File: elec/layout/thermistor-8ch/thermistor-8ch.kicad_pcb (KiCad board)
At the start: 4 copper layers, 29.7 x 28.3 mm, 78 parts, among them U5 10µH ±20%

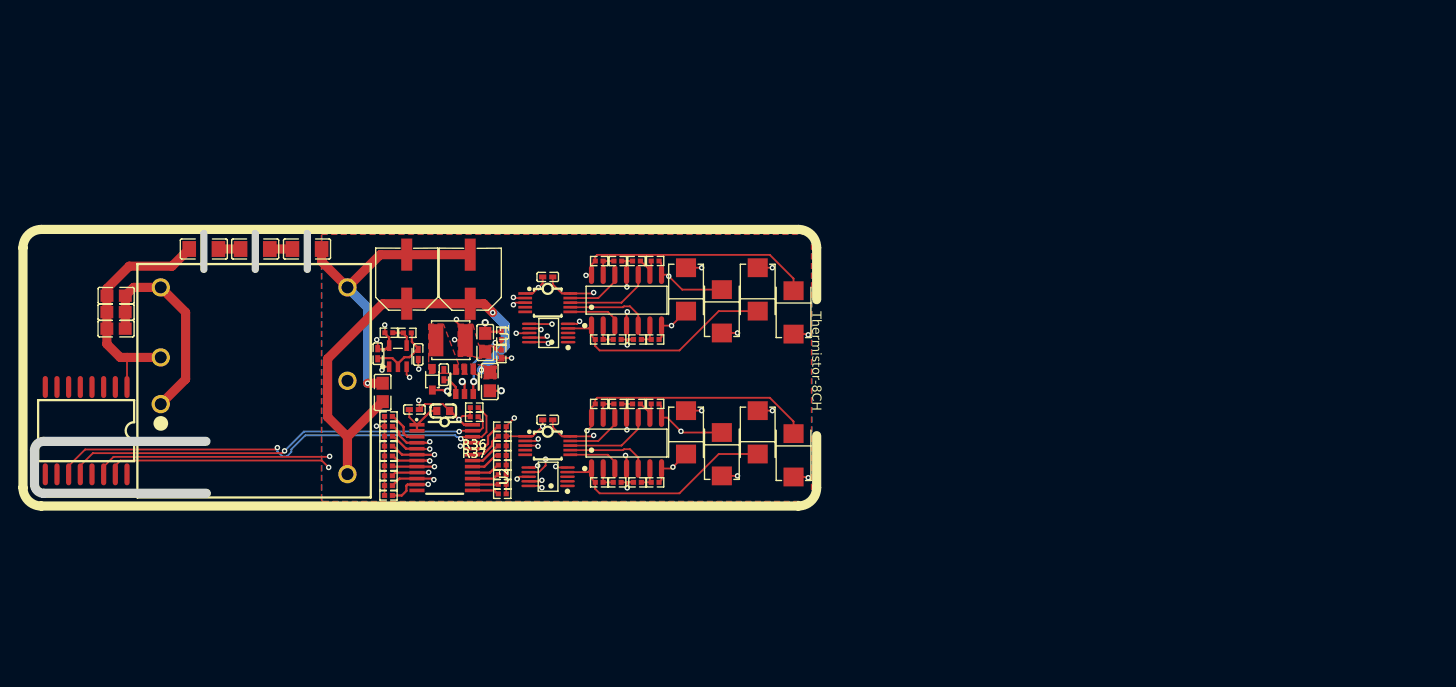
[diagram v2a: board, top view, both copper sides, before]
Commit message: add ATX core block
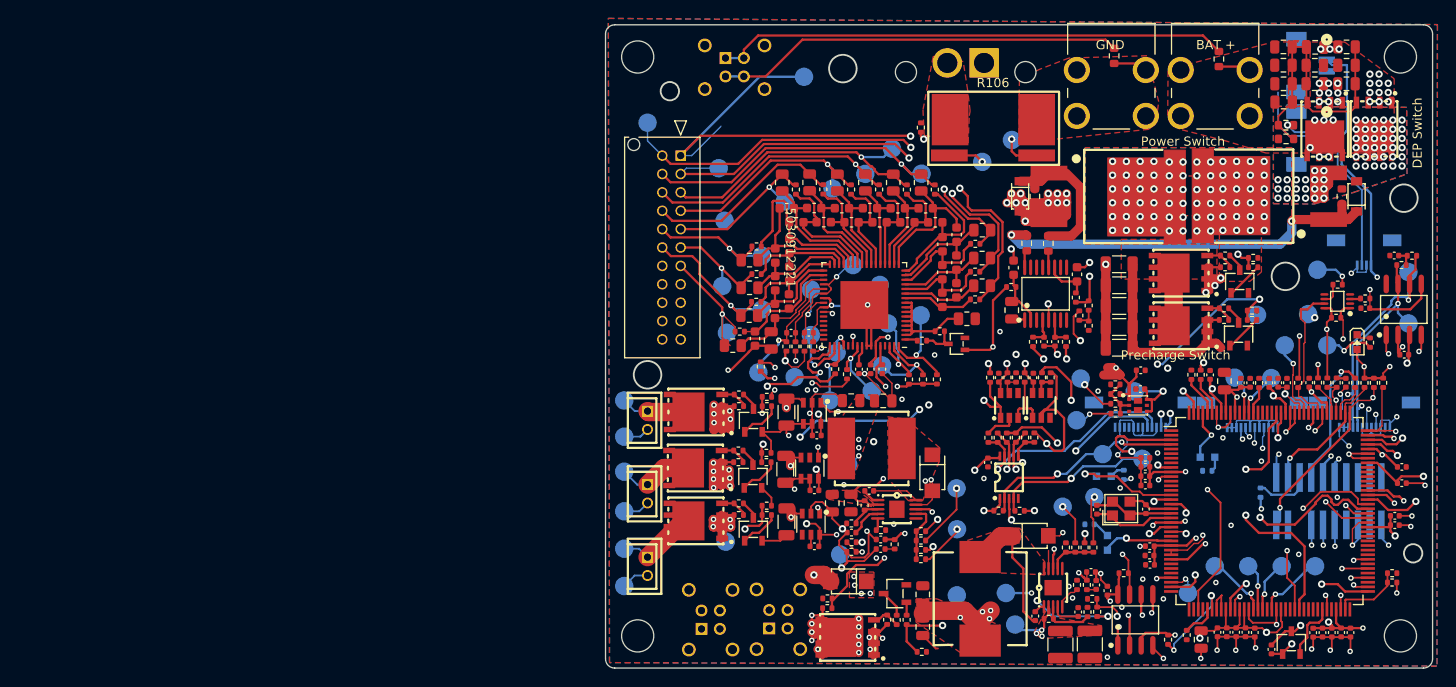
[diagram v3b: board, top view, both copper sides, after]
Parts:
- removed D5, D6, D7, D8: , atopile:SMB_L4.6-W3.6-LS5.3-RD-330cb3
- added C100: 16V 100nF X7R ±10% 0402 Multilayer Ceramic Capacitors MLCC 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, lib:C0402, F.Cu at (174.6, 105.3)
- added C101: 16V 100nF X7R ±10% 0402 Multilayer Ceramic Capacitors MLCC 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, lib:C0402, F.Cu at (175.0, 112.9)
- added C102: 16V 100nF X7R ±10% 0402 Multilayer Ceramic Capacitors MLCC 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, lib:C0402, F.Cu at (194.9, 121.3)
- added C103: 16V 100nF X7R ±10% 0402 Multilayer Ceramic Capacitors MLCC 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, lib:C0402, F.Cu at (202.7, 91.0)
- added C104: 16V 100nF X7R ±10% 0402 Multilayer Ceramic Capacitors MLCC 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, lib:C0402, F.Cu at (198.5, 86.0)
- added C105: 50V 4.7nF X7R ±10% 0402 Multilayer Ceramic Capacitors MLCC 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, lib:C0402, F.Cu at (201.7, 80.2)
- added C106: 16V 100nF X7R ±10% 0402 Multilayer Ceramic Capacitors MLCC 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, lib:C0402, F.Cu at (157.4, 102.8)
- added C107: 16V 100nF X7R ±10% 0402 Multilayer Ceramic Capacitors MLCC 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, lib:C0402, F.Cu at (170.4, 116.7)
- added C108: 16V 100nF X7R ±10% 0402 Multilayer Ceramic Capacitors MLCC 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, lib:C0402, F.Cu at (158.6, 93.5)
- added C109: 16V 100nF X7R ±10% 0402 Multilayer Ceramic Capacitors MLCC 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, lib:C0402, F.Cu at (162.4, 93.5)
- added C19: 25V 1uF X5R ±10% 0402 Multilayer Ceramic Capacitors MLCC - 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, lib:C0402, F.Cu at (174.0, 94.8)
- added C20: 25V 1uF X5R ±10% 0402 Multilayer Ceramic Capacitors MLCC - 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, lib:C0402, F.Cu at (174.1, 92.7)
- added C21: 25V 10uF X5R ±10% 0805 Multilayer Ceramic Capacitors MLCC -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, lib:C0805, F.Cu at (150.3, 117.1)
- added C22: 25V 10uF X5R ±10% 0805 Multilayer Ceramic Capacitors MLCC -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, lib:C0805, F.Cu at (150.3, 120.6)
- added C23: ?, lib:C1210, F.Cu at (168.5, 122.6)
- added C24: ?, lib:C1210, F.Cu at (165.3, 122.6)
- added C25: 50V 10nF X7R ±10% 0402 Multilayer Ceramic Capacitors MLCC -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, lib:C0402, F.Cu at (167.3, 119.0)
- added C26: 16V 100nF X7R ±10% 0402 Multilayer Ceramic Capacitors MLCC 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, lib:C0402, F.Cu at (162.6, 119.5)
- added C27: 16V 68nF X7R ±10% 0402 Multilayer Ceramic Capacitors MLCC -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, lib:C0402, F.Cu at (169.2, 116.1)
- added C28: 50V 6.8nF X7R ±10% 0402 Multilayer Ceramic Capacitors MLCC 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, lib:C0402, F.Cu at (168.7, 114.7)
- added C29: 25V 1uF X5R ±10% 0402 Multilayer Ceramic Capacitors MLCC - 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, lib:C0402, F.Cu at (145.9, 92.6)
- added C30: 25V 1uF X5R ±10% 0402 Multilayer Ceramic Capacitors MLCC - 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, lib:C0402, F.Cu at (143.4, 92.6)
- added C31: 25V 1uF X5R ±10% 0402 Multilayer Ceramic Capacitors MLCC - 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, lib:C0402, F.Cu at (144.7, 92.6)
- added C32: 50V 10nF X7R ±10% 0603 Multilayer Ceramic Capacitors MLCC -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, lib:C0603, F.Cu at (135.8, 85.2)
- added C33: 50V 27nF X7R ±10% 0603 Multilayer Ceramic Capacitors MLCC -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, lib:C0603, F.Cu at (134.3, 86.3)
- added C34: 50V 100nF X7R ±10% 0805 Multilayer Ceramic Capacitors MLCC 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, lib:C0805, F.Cu at (133.8, 89.5)
- added C35: 50V 10nF X7R ±10% 0603 Multilayer Ceramic Capacitors MLCC -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, lib:C0603, F.Cu at (132.1, 89.3)
- added C36: 50V 10nF X7R ±10% 0603 Multilayer Ceramic Capacitors MLCC -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, lib:C0603, F.Cu at (135.8, 82.2)
- added C37: 50V 27nF X7R ±10% 0603 Multilayer Ceramic Capacitors MLCC -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, lib:C0603, F.Cu at (134.3, 83.3)
- added C38: 50V 10nF X7R ±10% 0603 Multilayer Ceramic Capacitors MLCC -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, lib:C0603, F.Cu at (135.8, 79.2)
- added C39: 50V 27nF X7R ±10% 0603 Multilayer Ceramic Capacitors MLCC -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, lib:C0603, F.Cu at (134.3, 80.2)
- added C40: 50V 10nF X7R ±10% 0603 Multilayer Ceramic Capacitors MLCC -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, lib:C0603, F.Cu at (136.6, 76.6)
- added C41: 50V 27nF X7R ±10% 0603 Multilayer Ceramic Capacitors MLCC -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, lib:C0603, F.Cu at (135.5, 75.1)
- added C42: 50V 10nF X7R ±10% 0603 Multilayer Ceramic Capacitors MLCC -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, lib:C0603, F.Cu at (139.6, 76.6)
- added C43: 50V 27nF X7R ±10% 0603 Multilayer Ceramic Capacitors MLCC -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, lib:C0603, F.Cu at (138.5, 75.1)
- added C44: 50V 10nF X7R ±10% 0603 Multilayer Ceramic Capacitors MLCC -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, lib:C0603, F.Cu at (142.6, 76.6)
- added C45: 50V 27nF X7R ±10% 0603 Multilayer Ceramic Capacitors MLCC -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, lib:C0603, F.Cu at (141.6, 75.1)
- added C46: 50V 10nF X7R ±10% 0603 Multilayer Ceramic Capacitors MLCC -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, lib:C0603, F.Cu at (145.6, 76.6)
- added C47: 50V 27nF X7R ±10% 0603 Multilayer Ceramic Capacitors MLCC -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, lib:C0603, F.Cu at (144.6, 75.1)
- added C48: 50V 10nF X7R ±10% 0603 Multilayer Ceramic Capacitors MLCC -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, lib:C0603, F.Cu at (148.7, 76.6)
- added C49: 50V 27nF X7R ±10% 0603 Multilayer Ceramic Capacitors MLCC -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, lib:C0603, F.Cu at (147.6, 75.1)
- added C50: 50V 10nF X7R ±10% 0603 Multilayer Ceramic Capacitors MLCC -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, lib:C0603, F.Cu at (151.7, 76.6)
- added C51: 50V 27nF X7R ±10% 0603 Multilayer Ceramic Capacitors MLCC -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, lib:C0603, F.Cu at (150.7, 75.1)
- added C52: 50V 10nF X7R ±10% 0603 Multilayer Ceramic Capacitors MLCC -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, lib:C0603, F.Cu at (152.5, 79.0)
- added C53: 50V 27nF X7R ±10% 0603 Multilayer Ceramic Capacitors MLCC -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, lib:C0603, F.Cu at (154.0, 78.0)
- added C54: 50V 10nF X7R ±10% 0603 Multilayer Ceramic Capacitors MLCC -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, lib:C0603, F.Cu at (152.5, 82.1)
- added C55: 50V 27nF X7R ±10% 0603 Multilayer Ceramic Capacitors MLCC -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, lib:C0603, F.Cu at (154.0, 81.0)
- added C56: 50V 10nF X7R ±10% 0603 Multilayer Ceramic Capacitors MLCC -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, lib:C0603, F.Cu at (152.5, 85.1)
- added C57: 50V 27nF X7R ±10% 0603 Multilayer Ceramic Capacitors MLCC -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, lib:C0603, F.Cu at (154.0, 84.0)
- added C58: ?, lib:R0805, F.Cu at (155.1, 87.1)
- added C59: 50V 10nF X7R ±10% 0402 Multilayer Ceramic Capacitors MLCC -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, lib:C0402, F.Cu at (137.9, 88.6)
- added C60: 50V 10nF X7R ±10% 0402 Multilayer Ceramic Capacitors MLCC -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, lib:C0402, F.Cu at (136.0, 88.6)
- added C61: 50V 10nF X7R ±10% 0603 Multilayer Ceramic Capacitors MLCC -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, lib:C0603, F.Cu at (160.2, 81.6)
- added C62: 50V 10nF X7R ±10% 0603 Multilayer Ceramic Capacitors MLCC -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, lib:C0603, F.Cu at (167.1, 82.3)
- added C63: 16V 100nF X7R ±10% 0402 Multilayer Ceramic Capacitors MLCC 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, lib:C0402, F.Cu at (163.5, 89.6)
- added C64: 16V 100nF X7R ±10% 0402 Multilayer Ceramic Capacitors MLCC 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, lib:C0402, F.Cu at (164.7, 89.6)
- added C65: 50V 1uF X7R ±10% 0805 Multilayer Ceramic Capacitors MLCC - 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, lib:C0805, F.Cu at (160.0, 86.2)
- added C66: 25V 1uF X5R ±10% 0402 Multilayer Ceramic Capacitors MLCC - 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, lib:C0402, F.Cu at (138.6, 111.9)
- added C67: 25V 1uF X5R ±10% 0402 Multilayer Ceramic Capacitors MLCC - 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, lib:C0402, F.Cu at (138.6, 105.8)
- added C68: 25V 1uF X5R ±10% 0402 Multilayer Ceramic Capacitors MLCC - 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, lib:C0402, F.Cu at (138.8, 99.8)
- added C69: 16V 100nF X7R ±10% 0402 Multilayer Ceramic Capacitors MLCC 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, lib:C0402, F.Cu at (188.3, 123.1)
- added C70: 50V 20pF C0G ±5% 0402 Multilayer Ceramic Capacitors MLCC - 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, lib:C0402, F.Cu at (169.3, 107.9)
- added C71: 50V 20pF C0G ±5% 0402 Multilayer Ceramic Capacitors MLCC - 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, lib:C0402, F.Cu at (174.6, 107.8)
- added C72: 16V 100nF X7R ±10% 0402 Multilayer Ceramic Capacitors MLCC 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, lib:C0402, F.Cu at (174.6, 102.3)
- added C73: 50V 20pF C0G ±5% 0402 Multilayer Ceramic Capacitors MLCC - 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, lib:C0402, F.Cu at (196.4, 94.1)
- added C74: 25V 22uF X5R ±20% 0805 Multilayer Ceramic Capacitors MLCC -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, lib:C0805, F.Cu at (180.6, 122.0)
- added C75: 16V 100nF X7R ±10% 0402 Multilayer Ceramic Capacitors MLCC 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, lib:C0402, F.Cu at (192.4, 94.1)
- added C76: 16V 100nF X7R ±10% 0402 Multilayer Ceramic Capacitors MLCC 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, lib:C0402, F.Cu at (186.5, 121.3)
- added C77: 16V 100nF X7R ±10% 0402 Multilayer Ceramic Capacitors MLCC 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, lib:C0402, F.Cu at (188.0, 94.1)
- added C78: 16V 100nF X7R ±10% 0402 Multilayer Ceramic Capacitors MLCC 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, lib:C0402, F.Cu at (181.6, 93.2)
- added C79: 16V 100nF X7R ±10% 0402 Multilayer Ceramic Capacitors MLCC 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, lib:C0402, F.Cu at (201.7, 109.6)
- added C80: 16V 100nF X7R ±10% 0402 Multilayer Ceramic Capacitors MLCC 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, lib:C0402, F.Cu at (201.7, 108.6)
- added C81: 16V 100nF X7R ±10% 0402 Multilayer Ceramic Capacitors MLCC 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, lib:C0402, F.Cu at (184.4, 121.2)
- added C82: 16V 100nF X7R ±10% 0402 Multilayer Ceramic Capacitors MLCC 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, lib:C0402, F.Cu at (183.4, 121.2)
- added C83: 16V 100nF X7R ±10% 0402 Multilayer Ceramic Capacitors MLCC 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, lib:C0402, F.Cu at (182.4, 121.2)
- added C84: 16V 100nF X7R ±10% 0402 Multilayer Ceramic Capacitors MLCC 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, lib:C0402, F.Cu at (202.5, 105.0)
- added C85: 16V 100nF X7R ±10% 0402 Multilayer Ceramic Capacitors MLCC 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, lib:C0402, F.Cu at (185.5, 121.2)
- added C86: 25V 22uF X5R ±20% 0805 Multilayer Ceramic Capacitors MLCC -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, lib:C0805, F.Cu at (183.2, 93.9)
- added C87: 16V 100nF X7R ±10% 0402 Multilayer Ceramic Capacitors MLCC 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, lib:C0402, F.Cu at (174.6, 103.2)
- added C88: 16V 100nF X7R ±10% 0402 Multilayer Ceramic Capacitors MLCC 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, lib:C0402, F.Cu at (175.1, 113.9)
- added C89: 16V 100nF X7R ±10% 0402 Multilayer Ceramic Capacitors MLCC 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, lib:C0402, F.Cu at (193.8, 121.3)
- added C90: 16V 100nF X7R ±10% 0402 Multilayer Ceramic Capacitors MLCC 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, lib:C0402, F.Cu at (185.0, 94.1)
- added C91: 16V 100nF X7R ±10% 0402 Multilayer Ceramic Capacitors MLCC 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, lib:C0402, F.Cu at (192.8, 121.3)
- added C92: 16V 100nF X7R ±10% 0402 Multilayer Ceramic Capacitors MLCC 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, lib:C0402, F.Cu at (186.0, 94.1)
- added C93: 16V 100nF X7R ±10% 0402 Multilayer Ceramic Capacitors MLCC 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, lib:C0402, F.Cu at (202.5, 103.2)
- added C94: 16V 100nF X7R ±10% 0402 Multilayer Ceramic Capacitors MLCC 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, lib:C0402, F.Cu at (189.0, 94.1)
- added C95: 16V 100nF X7R ±10% 0402 Multilayer Ceramic Capacitors MLCC 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, lib:C0402, F.Cu at (195.9, 121.3)
- added C96: 16V 100nF X7R ±10% 0402 Multilayer Ceramic Capacitors MLCC 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, lib:C0402, F.Cu at (190.0, 94.1)
- added C97: 16V 100nF X7R ±10% 0402 Multilayer Ceramic Capacitors MLCC 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, lib:C0402, F.Cu at (196.9, 121.3)
- added C98: 16V 100nF X7R ±10% 0402 Multilayer Ceramic Capacitors MLCC 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, lib:C0402, F.Cu at (175.0, 111.9)
- added C99: 16V 100nF X7R ±10% 0402 Multilayer Ceramic Capacitors MLCC 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, lib:C0402, F.Cu at (174.6, 104.2)
- added DZ1: ?, lib:SOD-123_L2.7-W1.6-LS3.7-RD, F.Cu at (160.9, 73.8)
- added DZ2: ?, lib:SOD-123_L2.7-W1.6-LS3.7-RD, F.Cu at (197.6, 73.8)
- added J1: ?, lib:SAMTEC_FTR-110-03-G-D-06, B.Cu at (194.5, 107.0)
- added L1: ?, lib:IND-SMD_L8.0-W8.0_SMNR8040, F.Cu at (144.8, 101.2)
- added L2: ?, lib:IND-SMD_L10.1-W10.1_SMDRS1045, F.Cu at (156.6, 117.6)
- added LED1: ?, lib:LED0603-RD, B.Cu at (170.4, 111.5)
- added LED2: ?, lib:LED0603-RD, B.Cu at (170.1, 104.3)
- added Q1: ?, lib:POWERPAK-SO-8_L6.1-W5.1-P1.27-BL-EP, F.Cu at (199.5, 66.5)
- added Q10: ?, lib:SOT-23-3_L2.9-W1.6-P1.90-LS2.8-BR, F.Cu at (131.9, 110.0)
- added Q11: ?, lib:POWERPAK-SO-8_L6.1-W5.1-P1.27-BL-EP, F.Cu at (125.6, 103.4)
- added Q12: ?, lib:SOT-23-3_L2.9-W1.6-P1.90-LS2.8-BR, F.Cu at (131.9, 104.3)
- added Q13: ?, lib:POWERPAK-SO-8_L6.1-W5.1-P1.27-BL-EP, F.Cu at (125.7, 97.3)
- added Q14: ?, lib:SOT-23-3_L2.9-W1.6-P1.90-LS2.8-BR, F.Cu at (131.9, 98.2)
- added Q15: ?, lib:POWERPAK-SO-8_L6.1-W5.1-P1.27-BL-EP, F.Cu at (142.2, 121.8)
- added Q16: ?, lib:SOT-23-3_L2.9-W1.6-P1.90-LS2.8-BR, F.Cu at (147.3, 117.0)
- added Q2: ?, lib:POWERPAK-SO-8_L6.1-W5.1-P1.27-BL-EP, F.Cu at (194.1, 66.5)
- added Q3: ?, lib:TO-263-3_L10.1-W9.0-P5.08-LS15.2-BL-1, F.Cu at (189.2, 73.8)
- added Q4: ?, lib:TO-263-3_L10.1-W9.0-P5.08-LS15.2-BL-1, F.Cu at (169.4, 73.8)
- added Q5: ?, lib:POWERPAK-SO-8_L6.1-W5.1-P1.27-BL-EP, F.Cu at (178.5, 87.9)
- added Q6: ?, lib:SOT-23-3_L2.9-W1.6-P1.90-LS2.8-BR, F.Cu at (184.7, 88.8)
- added Q7: ?, lib:POWERPAK-SO-8_L6.1-W5.1-P1.27-BL-EP, F.Cu at (178.4, 82.2)
- added Q8: ?, lib:SOT-23-3_L2.9-W1.6-P1.90-LS2.8-BR, F.Cu at (184.8, 83.1)
- added Q9: ?, lib:POWERPAK-SO-8_L6.1-W5.1-P1.27-BL-EP, F.Cu at (125.7, 109.1)
- added R100: ?, lib:R1206, F.Cu at (135.4, 103.5)
- added R101: 62.5mW Thick Film Resistors 50V ±100ppm/℃ ±1% 39kΩ 0402 Chi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, lib:R0402, F.Cu at (130.3, 96.6)
- added R102: 62.5mW Thick Film Resistors 50V ±100ppm/℃ ±1% 120kΩ 0402 Ch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, lib:R0402, F.Cu at (130.3, 95.4)
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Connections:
- C1 pad 1: CB -> battery-vcc
- C1 pad 2: SW -> inhibit_switch-gate
- C10 pad 1: hv-2 -> battery-vcc
- C10 pad 2: gnd -> inhibit_switch-gate
- C11 pad 1: hv-2 -> 1v2_vcc
- C12 pad 1: hv-2 -> 1v2_vcc
- C13 pad 1: hv-4 -> 5v_vcc
- C13 pad 2: gnd-1 -> gnd
- C14 pad 1: hv-4 -> 5v_vcc
- C14 pad 2: gnd-1 -> gnd
- C15 pad 1: hv-4 -> power_supply_1v2.ic-ss_tr
- C15 pad 2: gnd-1 -> gnd
- C16 pad 1: gnd -> power_supply_1v2.ic-boot
- C16 pad 2: regulator_24v_isolated-net-1 -> power_supply_1v2.ic-ph
- C17 pad 1: regulator_24v_isolated-net-1 -> power_supply_1v2.r_comp-vcc
- C17 pad 2: regulator_24v_isolated-net -> gnd
- C18 pad 1: regulator_24v_isolated-net -> power_supply_1v2.ic-comp
- C18 pad 2: gnd-1 -> gnd
- C2 pad 1: hv-4 -> battery-vcc
- C2 pad 2: gnd-1 -> inhibit_switch-gate
- C3 pad 1: hv -> battery-vcc
- C3 pad 2: gnd-1 -> inhibit_switch-gate
- C4 pad 1: hv-1 -> battery-vcc
- C4 pad 2: gnd-1 -> inhibit_switch-gate
- C5 pad 1: hv-1 -> battery-vcc
- C5 pad 2: gnd-1 -> inhibit_switch-gate
- C6 pad 1: hv-1 -> battery-vcc
- C6 pad 2: gnd-1 -> inhibit_switch-gate
- C7 pad 1: hv-1 -> battery-vcc
- C7 pad 2: gnd-1 -> inhibit_switch-gate
- C8 pad 1: hv -> battery-vcc
- C8 pad 2: gnd-1 -> inhibit_switch-gate
- C9 pad 1: hv-1 -> battery-vcc
- C9 pad 2: gnd-1 -> inhibit_switch-gate
- D1 pad 1: line-8 -> power_supply_1v2.ic-ph
- D1 pad 2: gnd-1 -> gnd
- D2 pad 1: line-12 -> power_supply_5v.ic-ph
- D2 pad 2: gnd-1 -> gnd
- D3 pad 1: line-17 -> batt_inhibit_vcc
- D3 pad 2: gnd-1 -> (no net)
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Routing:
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- added copper zone on F.Cu, net 1v2_vcc
- added copper zone on In1.Cu, net 1v2_vcc
- added copper zone on In3.Cu, net 1v2_vcc
- added copper zone on In2.Cu, net 3v3_vcc
- added copper zone on In4.Cu, net 3v3_vcc
- added copper zone on F.Cu, net 5v_vcc
- added copper zone on B.Cu, net batt_inhibit_vcc
- added copper zone on F.Cu, net batt_inhibit_vcc
- added copper zone on In1.Cu, net batt_inhibit_vcc
- added copper zone on In1.Cu, net batt_sat_vcc
- added copper zone on In2.Cu, net batt_sat_vcc
- added copper zone on In1.Cu, net batt_share_vcc
- added copper zone on In2.Cu, net batt_share_vcc
- added copper zone on F.Cu, net batt_system_vcc
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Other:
- board size 29.7 x 28.3 mm -> 90 x 70 mm
- copper layers 4 -> 6
- board text added: "1V2"
- board text added: "5V"
- board text added: "BAT +"
- board text added: "Batt Sense"
- board text added: "C0"
- board text added: "C1"
- board text added: "C10"
- board text added: "C11"
- board text added: "C12"
- board text added: "C2"
- board text added: "C4"
- board text added: "C5"
- board text added: "C6"
- board text added: "C7"
- board text added: "C8"
- board text added: "C9"
- board text added: "CAN"
- board text added: "CANH"
- board text added: "CANL"
- board text added: "CS"
- board text added: "DEBUG"
- board text added: "DEP"
- board text added: "DEP Switch"
- board text added: "ECLK"
- board text added: "GND"
- board text added: "Housekeeper"
- board text added: "I1N"
- board text added: "I1P"
- board text added: "I2N"
- board text added: "I2P"
- board text added: "Inhibit"
- board text added: "MISO"
- board text added: "MOSI"
- board text added: "MPSpace"
- board text added: "PCDU"
- board text added: "POR"
- board text added: "Power Switch"
- board text added: "Precharge Switch"
- board text added: "REV04.1"
- board text added: "RST"
- board text added: "RX"
- board text added: "SCK"
- board text added: "SCL"
- board text added: "SDA"
- board text added: "SEP"
- board text added: "SERIAL"
- board text added: "SHNTN"
- board text added: "SHNTP"
- board text added: "SPI1"
- board text added: "SPI3"
- board text added: "STATUS"
- board text added: "T0"
- board text added: "T1"
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
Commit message: remove omron relay, fix thermistor layout
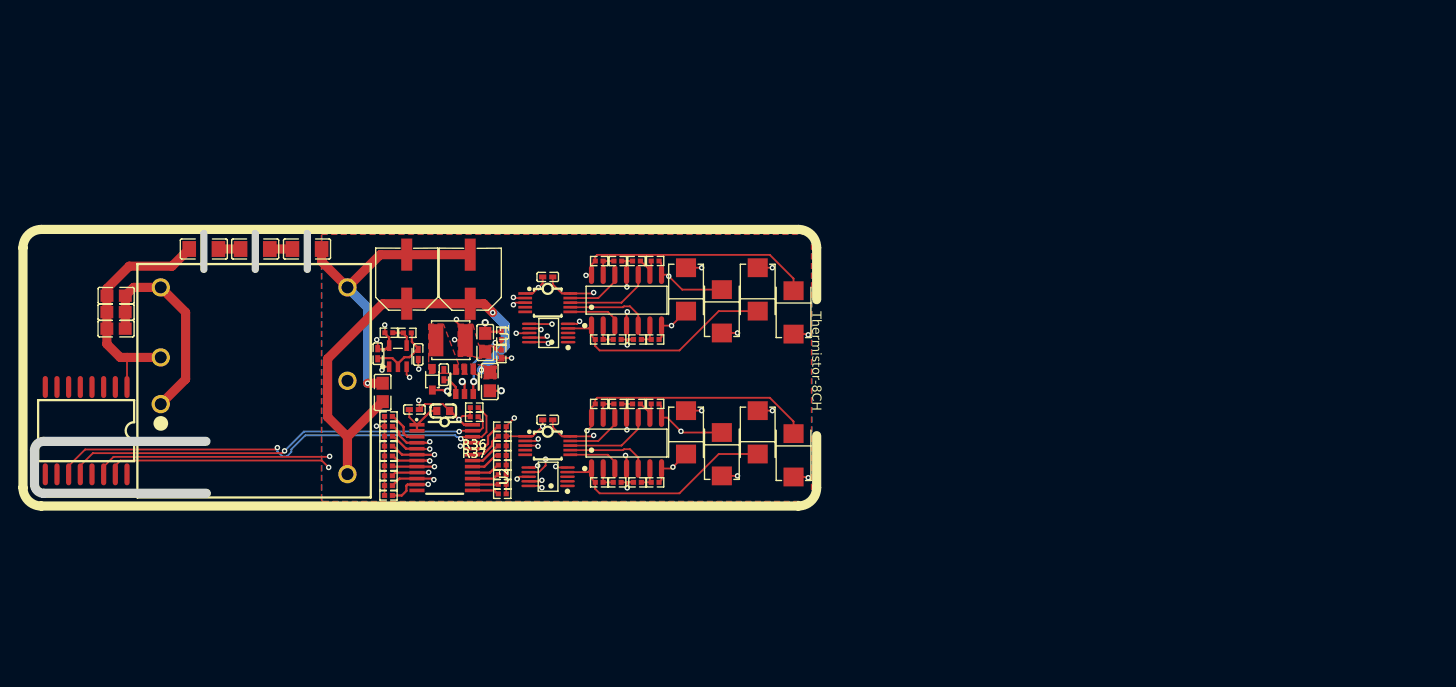
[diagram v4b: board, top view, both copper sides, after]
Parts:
- removed C100, C101, C102, C103, C104, C106, C107, C108, C109, C26, C63, C64, C69, C72, C75, C76, C77, C78, C79, C80, C81, C82, C83, C84, C85, C87, C88, C89, C90, C91, C92, C93, C94, C95, C96, C97, C98, C99: 16V 100nF X7R ±10% 0402 Multilayer Ceramic Capacitors MLCC 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, lib:C0402
- removed C105: 50V 4.7nF X7R ±10% 0402 Multilayer Ceramic Capacitors MLCC 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, lib:C0402
- removed C19, C20, C29, C30, C31, C66, C67, C68: 25V 1uF X5R ±10% 0402 Multilayer Ceramic Capacitors MLCC - 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, lib:C0402
- removed C21, C22: 25V 10uF X5R ±10% 0805 Multilayer Ceramic Capacitors MLCC -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, lib:C0805
- removed C23, C24: ?, lib:C1210
- removed C25, C59, C60: 50V 10nF X7R ±10% 0402 Multilayer Ceramic Capacitors MLCC -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, lib:C0402
- removed C27: 16V 68nF X7R ±10% 0402 Multilayer Ceramic Capacitors MLCC -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, lib:C0402
- removed C28: 50V 6.8nF X7R ±10% 0402 Multilayer Ceramic Capacitors MLCC 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, lib:C0402
- removed C32, C35, C36, C38, C40, C42, C44, C46, C48, C50, C52, C54, C56, C61, C62: 50V 10nF X7R ±10% 0603 Multilayer Ceramic Capacitors MLCC -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, lib:C0603
- removed C33, C37, C39, C41, C43, C45, C47, C49, C51, C53, C55, C57: 50V 27nF X7R ±10% 0603 Multilayer Ceramic Capacitors MLCC -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, lib:C0603
- removed C34: 50V 100nF X7R ±10% 0805 Multilayer Ceramic Capacitors MLCC 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, lib:C0805
- removed C58: ?, lib:R0805
- removed C65: 50V 1uF X7R ±10% 0805 Multilayer Ceramic Capacitors MLCC - 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, lib:C0805
- removed C70, C71, C73: 50V 20pF C0G ±5% 0402 Multilayer Ceramic Capacitors MLCC - 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, lib:C0402
- removed C74, C86: 25V 22uF X5R ±20% 0805 Multilayer Ceramic Capacitors MLCC -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, lib:C0805
- removed DZ1, DZ2: ?, lib:SOD-123_L2.7-W1.6-LS3.7-RD
- removed J1: ?, lib:SAMTEC_FTR-110-03-G-D-06
- removed L1: ?, lib:IND-SMD_L8.0-W8.0_SMNR8040
- removed L2: ?, lib:IND-SMD_L10.1-W10.1_SMDRS1045
- removed LED1, LED2, U83, U84: ?, lib:LED0603-RD
- removed Q1, Q11, Q13, Q15, Q2, Q5, Q7, Q9: ?, lib:POWERPAK-SO-8_L6.1-W5.1-P1.27-BL-EP
- removed Q10, Q12, Q14, Q16, Q6, Q8, U67: ?, lib:SOT-23-3_L2.9-W1.6-P1.90-LS2.8-BR
- removed Q3, Q4: ?, lib:TO-263-3_L10.1-W9.0-P5.08-LS15.2-BL-1
- removed R100, R105, R86, R87, R88, R89, R90, R95: ?, lib:R1206
- removed R101, R144, R78, R82, R91, R96: 62.5mW Thick Film Resistors 50V ±100ppm/℃ ±1% 39kΩ 0402 Chi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, lib:R0402
- removed R102, R145, R79, R83, R92, R97: 62.5mW Thick Film Resistors 50V ±100ppm/℃ ±1% 120kΩ 0402 Ch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, lib:R0402
- removed R103, R111, R112, R113, R115, R116, R117, R121, R122, R129, R130, R131, R134, R136, R146, R150, R151, R152, R153, R80, R84, R93, R98: 62.5mW Thick Film Resistors 50V ±100ppm/℃ ±1% 10kΩ 0402 Chi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, lib:R0402
- removed R104, R147, R81, R85, R94, R99: 62.5mW Thick Film Resistors 50V ±100ppm/℃ ±1% 1kΩ 0402 Chip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, lib:R0402
- removed R106: ?, lib:RES-SMD_4P-L10.8-W6.7
- removed R107, R108: 62.5mW Thick Film Resistors 50V ±1% ±100ppm/℃ 22Ω 0402 Chip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, lib:R0402
- removed R109, R118, R59, R70, R71: 62.5mW Thick Film Resistors 50V ±1% ±200ppm/℃ 100Ω 0402 Chi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, lib:R0402
- removed R110, R114, R72, R73: 62.5mW Thick Film Resistors 50V ±100ppm/℃ ±1% 4.7kΩ 0402 Ch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, lib:R0402
- removed R119, R120, R127, R128: 62.5mW Thick Film Resistors 50V ±100ppm/℃ ±1% 62Ω 0402 Chip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, lib:R0402
- removed R123, R124, R125, R126: 62.5mW Thick Film Resistors 50V ±100ppm/℃ ±1% 300Ω 0402 Chi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, lib:R0402
- removed R132: 62.5mW Thick Film Resistors 50V ±100ppm/℃ ±1% 28kΩ 0402 Chi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, lib:R0402
- removed R133, R64, R65, R66, R67, R68: 62.5mW Thick Film Resistors 50V ±100ppm/℃ ±1% 100kΩ 0402 Ch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, lib:R0402
- removed R135: 62.5mW Thick Film Resistors 50V ±100ppm/℃ ±1% 24.9kΩ 0402 C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, lib:R0402
- removed R137: 62.5mW Thick Film Resistors 50V ±800ppm/℃ ±1% 0Ω 0402 Chip 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, lib:R0402
- removed R138: 62.5mW Thick Film Resistors 50V ±100ppm/℃ ±1% 9.1kΩ 0402 Ch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, lib:R0402
- removed R139: 62.5mW Thick Film Resistors 50V ±100ppm/℃ ±1% 12.4kΩ 0402 C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, lib:R0402
- removed R140: 62.5mW Thick Film Resistors 50V ±100ppm/℃ ±1% 3.6kΩ 0402 Ch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, lib:R0402
- removed R141: 62.5mW Thick Film Resistors 50V ±100ppm/℃ ±1% 3.83kΩ 0402 C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, lib:R0402
- removed R142: 62.5mW Thick Film Resistors 50V ±100ppm/℃ ±1% 1.07MΩ 0402 C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, lib:R0402
- removed R143: 62.5mW Thick Film Resistors 50V ±100ppm/℃ ±1% 80.6kΩ 0402 C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, lib:R0402
- removed R148: 62.5mW Thick Film Resistors 50V ±100ppm/℃ ±1% 91kΩ 0402 Chi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, lib:R0402
- removed R149: 62.5mW Thick Film Resistors 50V ±100ppm/℃ ±1% 3.9kΩ 0402 Ch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, lib:R0402
- removed R40, R42, R44, R46, R48, R50, R52, R54, R56, R58: 125mW Thin Film Resistor 150V ±1% ±25ppm/℃ 80.6Ω 0805 Chip 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, lib:R0805
- removed R41, R43, R45, R47, R49, R51, R53, R55, R57, R60, R61, R62, R63: 62.5mW Thick Film Resistors 50V ±100ppm/℃ ±1% 200Ω 0402 Chi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, lib:R0402
- removed R69: ?, lib:R0402
- removed R74, R75: 100mW Thick Film Resistors 75V ±1% ±200ppm/℃ 100Ω 0603 Chip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, lib:R0603
- removed R76, R77: 100mW Thick Film Resistors 75V ±100ppm/℃ ±1% 10MΩ 0603 Chip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, lib:R0603
- removed U100, U14, U15, U17, U19, U20, U21, U22, U24, U25, U26, U27, U28, U29, U30, U31, U32, U33, U34, U35, U36, U37, U38, U39, U40, U41, U42, U43, U44, U56, U57, U59, U60, U62, U63, U64, U65, U70, U71, U77, U78, U79, U80, U81, U82, U85, U86, U87, U88, U89, U90, U91, U92, U93, U94, U95, U96, U97, U98, U99: ?, TestPoint:TestPoint_Pad_D2.0mm
- removed U16: ?, lib:CON_5030912221_MOL
- removed U18: ?, lib:MSOP-10_L3.0-W3.0-P0.50-LS4.9-BL-EP
- removed U23: ?, lib:LFCSP-64-1EP_9x9mm_P0.5mm_EP5.21x5.21mm
- removed U45: ?, lib:TSSOP-16_L5.0-W4.4-P0.65-LS6.4-BL
- removed U46, U47: ?, lib:CON2_1X2_U_DF13
- removed U48: ?, lib:HARWIN_M80-5000000M5-02-PM3-00-000
- removed U49, U50: ?, lib:HARWIN_M80-8530445
- removed U51: ?, lib:CON_5051100492_MOL
- removed U52, U53, U54: ?, lib:CON_5051101292_MOL
- removed U55, U58, U61: ?, lib:SOT-23-6_L2.9-W1.6-P0.95-LS2.8-TL
- removed U66: ?, lib:LQFP-144_20x20mm_Pitch0.5mm
- removed U68: ?, lib:CRYSTAL-SMD_4P-L2.5-W2.0-BL
- removed U69: ?, lib:VSSOP-8_L2.3-W2.0-P0.50-LS3.1-BR
- removed U72, U74: ?, lib:SOIC-8_L4.9-W3.9-P1.27-LS6.0-BL
- removed U73: ?, lib:TSSOP-10_L3.0-W3.0-P0.50-LS4.9-BL
- removed U75, U76: ?, lib:SOT-23-6_L2.9-W1.6-P0.95-LS2.8-BR
- added D5: , atopile:SMB_L4.6-W3.6-LS5.3-RD-330cb3, F.Cu at (132.4, 99.5)
- added D6: , atopile:SMB_L4.6-W3.6-LS5.3-RD-330cb3, F.Cu at (124.6, 99.5)
- added D7: , atopile:SMB_L4.6-W3.6-LS5.3-RD-330cb3, F.Cu at (128.5, 101.9)
- added D8: , atopile:SMB_L4.6-W3.6-LS5.3-RD-330cb3, F.Cu at (136.3, 102.0)
- C1: value ? -> 470nF ±20% 16V X5R; footprint lib:C0805 -> atopile:C0402-b3ef17
- C10: value ? -> 10µF ±10% 50V X5R; footprint lib:C0805 -> atopile:C0805-3b2e55
- C11: value 6.3V 47uF X5R ±20% 0805 Multilayer Ceramic Capacitors MLCC - SMD/SMT ROHS -> 10µF ±10% 50V X5R; footprint lib:C0805 -> atopile:C0805-3b2e55
- C12: value 6.3V 47uF X5R ±20% 0805 Multilayer Ceramic Capacitors MLCC - SMD/SMT ROHS -> 1µF ±10% 50V X7R; footprint lib:C0805 -> atopile:C0805-3b2e55
- C13: value 25V 10uF X5R ±10% 0805 Multilayer Ceramic Capacitors MLCC - SMD/SMT ROHS -> 1µF ±10% 50V X7R; footprint lib:C0805 -> atopile:C0805-3b2e55
- C14: value 25V 10uF X5R ±10% 0805 Multilayer Ceramic Capacitors MLCC - SMD/SMT ROHS -> 100µF ±20%; footprint lib:C0805 -> atopile:CAP-SMD_BD6.3-L6.6-W6.6-FD-3e301d
- C15: value 50V 10nF X7R ±10% 0402 Multilayer Ceramic Capacitors MLCC - SMD/SMT ROHS -> 100µF ±20%; footprint lib:C0402 -> atopile:CAP-SMD_BD6.3-L6.6-W6.6-FD-3e301d
- C16: value 16V 100nF X7R ±10% 0402 Multilayer Ceramic Capacitors MLCC - SMD/SMT ROHS -> 2.2nF ±5% 1kV C0G; footprint lib:C0402 -> atopile:C1206-f0a137
- C17: value 50V 47nF X7R ±10% 0402 Multilayer Ceramic Capacitors MLCC - SMD/SMT ROHS -> 2.2nF ±5% 1kV C0G; footprint lib:C0402 -> atopile:C1206-f0a137
- C18: value 50V 220pF X7R ±10% 0402 Multilayer Ceramic Capacitors MLCC - SMD/SMT ROHS -> 2.2nF ±5% 1kV C0G; footprint lib:C0402 -> atopile:C1206-f0a137
- C2: value ? -> 4.7µF ±10% 25V X5R; footprint lib:C0805 -> atopile:C0805-3b2e55
- C3: value ? -> 10µF ±10% 25V X5R; footprint lib:C0805 -> atopile:C0805-3b2e55
- C4, C5, C6: value ? -> 100nF ±10% 16V X7R; footprint lib:C0805 -> atopile:C0402-b3ef17
- C7: value ? -> 2.2µF ±10% 25V X5R; footprint lib:C0805 -> atopile:C0603-bd72f6
- C8, C9: value ? -> 1µF ±10% 25V X5R; footprint lib:C0805 -> atopile:C0402-b3ef17
- D1, D2, D4: value ? -> (none); footprint lib:SMAF_L3.5-W2.6-LS4.7-RD -> atopile:SMB_L4.6-W3.6-LS5.3-RD-330cb3
- D3: value ? -> (none); footprint lib:SOT-323-3_L2.0-W1.3-P1.30-LS2.1-BR -> atopile:SMB_L4.6-W3.6-LS5.3-RD-330cb3
- R1: value 100mW Thick Film Resistors 75V ±100ppm/℃ ±1% 10kΩ 0603 Chip Resistor - Surface Mount ROHS -> 8.2kΩ ±1% 62.5mW; footprint lib:R0603 -> atopile:R0402-56259e
- R10: value 62.5mW Thick Film Resistors 50V ±100ppm/℃ ±1% 59kΩ 0402 Chip Resistor - Surface Mount ROHS -> 100Ω ±1% 62.5mW; footprint lib:R0402 -> atopile:R0402-56259e
- R11: value 62.5mW Thick Film Resistors 50V ±100ppm/℃ ±1% 887kΩ 0402 Chip Resistor - Surface Mount ROHS -> 100Ω ±1% 62.5mW; footprint lib:R0402 -> atopile:R0402-56259e
- R12: value 62.5mW Thick Film Resistors 50V ±100ppm/℃ ±1% 169kΩ 0402 Chip Resistor - Surface Mount ROHS -> 100Ω ±1% 62.5mW; footprint lib:R0402 -> atopile:R0402-56259e
- R13: value 62.5mW Thick Film Resistors 50V ±100ppm/℃ ±1% 73.2kΩ 0402 Chip Resistor - Surface Mount ROHS -> 100Ω ±1% 62.5mW; footprint lib:R0402 -> atopile:R0402-56259e
- R14: value 62.5mW Thick Film Resistors 50V ±100ppm/℃ ±1% 4.64kΩ 0402 Chip Resistor - Surface Mount ROHS -> 100Ω ±1% 62.5mW; footprint lib:R0402 -> atopile:R0402-56259e
- R15: value 62.5mW Thick Film Resistors 50V ±100ppm/℃ ±1% 36kΩ 0402 Chip Resistor - Surface Mount ROHS -> 100Ω ±1% 62.5mW; footprint lib:R0402 -> atopile:R0402-56259e
- R16: value 62.5mW Thick Film Resistors 50V ±100ppm/℃ ±1% 7.15kΩ 0402 Chip Resistor - Surface Mount ROHS -> 100Ω ±1% 62.5mW; footprint lib:R0402 -> atopile:R0402-56259e
- R17: value 62.5mW Thick Film Resistors 50V ±100ppm/℃ ±1% 133kΩ 0402 Chip Resistor - Surface Mount ROHS -> 100Ω ±1% 62.5mW; footprint lib:R0402 -> atopile:R0402-56259e
- R18: value 62.5mW Thick Film Resistors 50V ±100ppm/℃ ±1% 536kΩ 0402 Chip Resistor - Surface Mount ROHS -> 100Ω ±1% 62.5mW; footprint lib:R0402 -> atopile:R0402-56259e
- R19, R29: value 62.5mW Thick Film Resistors 50V ±100ppm/℃ ±1% 44.2kΩ 0402 Chip Resistor - Surface Mount ROHS -> 10kΩ ±1% 62.5mW; footprint lib:R0402 -> atopile:R0402-56259e
- R2: value 100mW Thick Film Resistors 75V ±100ppm/℃ ±1% 10kΩ 0603 Chip Resistor - Surface Mount ROHS -> 47kΩ ±1% 62.5mW; footprint lib:R0603 -> atopile:R0402-56259e
- R20: value 62.5mW Thick Film Resistors 50V ±100ppm/℃ ±1% 133kΩ 0402 Chip Resistor - Surface Mount ROHS -> 10kΩ ±1% 62.5mW; footprint lib:R0402 -> atopile:R0402-56259e
- R21: value 62.5mW Thick Film Resistors 50V ±100ppm/℃ ±1% 442kΩ 0402 Chip Resistor - Surface Mount ROHS -> 10kΩ ±1% 62.5mW; footprint lib:R0402 -> atopile:R0402-56259e
- R22: value 62.5mW Thick Film Resistors 50V ±100ppm/℃ ±1% 84.5kΩ 0402 Chip Resistor - Surface Mount ROHS -> 10kΩ ±1% 62.5mW; footprint lib:R0402 -> atopile:R0402-56259e
- R23: value 62.5mW Thick Film Resistors 50V ±100ppm/℃ ±1% 1.43MΩ 0402 Chip Resistor - Surface Mount ROHS -> 10kΩ ±1% 62.5mW; footprint lib:R0402 -> atopile:R0402-56259e
- R24: value 62.5mW Thick Film Resistors 50V ±100ppm/℃ ±1% 3.92MΩ 0402 Chip Resistor - Surface Mount ROHS -> 10kΩ ±1% 62.5mW; footprint lib:R0402 -> atopile:R0402-56259e
- R25, R26: value 62.5mW Thick Film Resistors 50V ±100ppm/℃ ±1% 26.1kΩ 0402 Chip Resistor - Surface Mount ROHS -> 10kΩ ±1% 62.5mW; footprint lib:R0402 -> atopile:R0402-56259e
- R27: value 62.5mW Thick Film Resistors 50V ±100ppm/℃ ±1% 887kΩ 0402 Chip Resistor - Surface Mount ROHS -> 10kΩ ±1% 62.5mW; footprint lib:R0402 -> atopile:R0402-56259e
- R28: value 62.5mW Thick Film Resistors 50V ±100ppm/℃ ±1% 169kΩ 0402 Chip Resistor - Surface Mount ROHS -> 10kΩ ±1% 62.5mW; footprint lib:R0402 -> atopile:R0402-56259e
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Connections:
- C1 pad 1: battery-vcc -> CB
- C1 pad 2: inhibit_switch-gate -> SW
- C10 pad 1: battery-vcc -> hv-2
- C10 pad 2: inhibit_switch-gate -> gnd-1
- C11 pad 1: 1v2_vcc -> hv-2
- C11 pad 2: gnd -> gnd-1
- C12 pad 1: 1v2_vcc -> hv-2
- C12 pad 2: gnd -> gnd-1
- C13 pad 1: 5v_vcc -> hv-1
- C14 pad 1: 5v_vcc -> hv-1
- C15 pad 1: power_supply_1v2.ic-ss_tr -> hv-1
- C16 pad 1: power_supply_1v2.ic-boot -> gnd-1
- C16 pad 2: power_supply_1v2.ic-ph -> regulator_24v_isolated-net-1
- C17 pad 1: power_supply_1v2.r_comp-vcc -> regulator_24v_isolated-net-1
- C17 pad 2: gnd -> regulator_24v_isolated-net
- C18 pad 1: power_supply_1v2.ic-comp -> regulator_24v_isolated-net
- C2 pad 1: battery-vcc -> hv-1
- C2 pad 2: inhibit_switch-gate -> gnd
- C3 pad 1: battery-vcc -> hv
- C3 pad 2: inhibit_switch-gate -> gnd
- C4 pad 1: battery-vcc -> hv-4
- C4 pad 2: inhibit_switch-gate -> gnd
- C5 pad 1: battery-vcc -> hv-4
- C5 pad 2: inhibit_switch-gate -> gnd
- C6 pad 1: battery-vcc -> hv-4
- C6 pad 2: inhibit_switch-gate -> gnd
- C7 pad 1: battery-vcc -> hv-4
- C7 pad 2: inhibit_switch-gate -> gnd
- C8 pad 1: battery-vcc -> hv
- C8 pad 2: inhibit_switch-gate -> gnd
- C9 pad 1: battery-vcc -> hv-4
- C9 pad 2: inhibit_switch-gate -> gnd
- D1 pad 1: power_supply_1v2.ic-ph -> line-2
- D2 pad 1: power_supply_5v.ic-ph -> line-4
- D3 pad 1: batt_inhibit_vcc -> line-8
- D3 pad 2: (no net) -> gnd
- D4 pad 1: batt_system_vcc -> line-11
- D4 pad 2: batt_inhibit_vcc -> gnd
- R1 pad 1: battery.vcc_sense_resistor-p1 -> FB
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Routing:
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- added copper zone on B.Cu, net (none)
- added copper zone on F.Cu, net SW
- added copper zone on In1.Cu, net gnd
- added copper zone on F.Cu, net hv-1
- added copper zone on In2.Cu, net hv-4
- removed copper zone on F.Cu, net 1v2_vcc
- removed copper zone on In1.Cu, net 1v2_vcc
- removed copper zone on In3.Cu, net 1v2_vcc
- removed copper zone on In2.Cu, net 3v3_vcc
- removed copper zone on In4.Cu, net 3v3_vcc
- removed copper zone on F.Cu, net 5v_vcc
- removed copper zone on B.Cu, net batt_inhibit_vcc
- removed copper zone on F.Cu, net batt_inhibit_vcc
- removed copper zone on In1.Cu, net batt_inhibit_vcc
- removed copper zone on In1.Cu, net batt_sat_vcc
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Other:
- board size 90 x 70 mm -> 29.7 x 28.3 mm
- copper layers 6 -> 4
- board text added: "Thermistor-8CH"
- board text removed: "1V2"
- board text removed: "5V"
- board text removed: "BAT +"
- board text removed: "Batt Sense"
- board text removed: "C0"
- board text removed: "C1"
- board text removed: "C10"
- board text removed: "C11"
- board text removed: "C12"
- board text removed: "C2"
- board text removed: "C4"
- board text removed: "C5"
- board text removed: "C6"
- board text removed: "C7"
- board text removed: "C8"
- board text removed: "C9"
- board text removed: "CAN"
- board text removed: "CANH"
- board text removed: "CANL"
- board text removed: "CS"
- board text removed: "DEBUG"
- board text removed: "DEP"
- board text removed: "DEP Switch"
- board text removed: "ECLK"
- board text removed: "GND"
- board text removed: "Housekeeper"
- board text removed: "I1N"
- board text removed: "I1P"
- board text removed: "I2N"
- board text removed: "I2P"
- board text removed: "Inhibit"
- board text removed: "MISO"
- board text removed: "MOSI"
- board text removed: "MPSpace"
- board text removed: "PCDU"
- board text removed: "POR"
- board text removed: "Power Switch"
- board text removed: "Precharge Switch"
- board text removed: "REV04.1"
- board text removed: "RST"
- board text removed: "RX"
- board text removed: "SCK"
- board text removed: "SCL"
- board text removed: "SDA"
- board text removed: "SEP"
- board text removed: "SERIAL"
- board text removed: "SHNTN"
- board text removed: "SHNTP"
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
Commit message: building locally to fix frozen builds
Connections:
- net IN1plus renamed dac_1_4-VOUTA
- net VOUTA renamed dac_5_8-VOUTA
- net dac_1_4-IN2plus renamed IN2plus
- net dac_1_4-VOUTC renamed VOUTC
- net dac_1_4-VOUTD renamed IN4plus
- net dac_5_8-IN2plus renamed VOUTB
- net dac_5_8-VOUTC renamed IN3plus
- net dac_5_8-VOUTD renamed VOUTD
- C10 pad 1: hv-2 -> hv
- C11 pad 1: hv-2 -> hv
- C12 pad 1: hv-2 -> hv
- C13 pad 1: hv-1 -> hv-4
- C14 pad 1: hv-1 -> hv-4
- C15 pad 1: hv-1 -> hv-4
- C2 pad 1: hv-1 -> hv-4
- C3 pad 1: hv -> hv-3
- C4 pad 1: hv-4 -> hv-2
- C5 pad 1: hv-4 -> hv-2
- C6 pad 1: hv-4 -> hv-2
- C7 pad 1: hv-4 -> hv-2
- C8 pad 1: hv -> hv-3
- C9 pad 1: hv-4 -> hv-2
- D1 pad 1: line-2 -> line-3
- D2 pad 1: line-4 -> line-13
- D3 pad 1: line-8 -> line-18
- D4 pad 1: line-11 -> line-14
- D5 pad 1: line-5 -> line-12
- D6 pad 1: line-19 -> line-16
- D7 pad 1: line-3 -> line
- D8 pad 1: line-18 -> line-11
- R11 pad 2: line-5 -> line-12
- R13 pad 2: line-19 -> line-16
- R15 pad 2: line-3 -> line
- R17 pad 2: line-18 -> line-11
- R19 pad 1: line-13 -> line-4
- R19 pad 2: hv-4 -> hv-2
- R2 pad 1: hv -> hv-3
- R20 pad 1: line-14 -> line-6
- R20 pad 2: hv-4 -> hv-2
- R21 pad 1: line-15 -> line-5
- R21 pad 2: hv-4 -> hv-2
- R22 pad 1: line-17 -> line-8
- R22 pad 2: hv-4 -> hv-2
- R23 pad 1: line-7 -> line-10
- R23 pad 2: hv-4 -> hv-2
- R24 pad 1: line -> line-15
- R24 pad 2: hv-4 -> hv-2
- R25 pad 1: line-1 -> line-19
- R25 pad 2: hv-4 -> hv-2
- R26 pad 1: line-16 -> line-9
- R26 pad 2: hv-4 -> hv-2
- R27 pad 2: hv-4 -> hv-2
- R28 pad 2: hv-4 -> hv-2
- R29 pad 2: hv-4 -> hv-2
- R3 pad 2: line-2 -> line-3
- R30 pad 2: hv-4 -> hv-2
- R31 pad 2: hv-4 -> hv-2
- R32 pad 2: hv-4 -> hv-2
- R33 pad 2: hv-4 -> hv-2
- R34 pad 2: hv-4 -> hv-2
- R35 pad 2: hv-4 -> hv-2
- R36 pad 1: line-6 -> line-2
- R36 pad 2: hv-4 -> hv-2
- R37 pad 1: line-10 -> line-7
- R37 pad 2: hv-4 -> hv-2
- R39 pad 1: hv-4 -> hv-2
- R5 pad 2: line-4 -> line-13
- R7 pad 2: line-8 -> line-18
- R9 pad 2: line-11 -> line-14
- U1 pad 10: line-1 -> line-19
- U1 pad 4: line-2 -> line-3
- U1 pad 5: line-4 -> line-13
- U1 pad 6: line-8 -> line-18
- U1 pad 7: line-11 -> line-14
- U1 pad 8: hv -> hv-3
- U1 pad 9: line-16 -> line-9
- U10 pad 11: line-6 -> line-2
- U10 pad 12: line-10 -> line-7
- U10 pad 14: hv-4 -> hv-2
- U10 pad 3: hv-3 -> hv-1
- U10 pad 5: line-9 -> line-1
- U10 pad 6: line-12 -> line-17
- U11 pad 10: line-16 -> line-9
- U11 pad 11: line-1 -> line-19
- U11 pad 22: line-6 -> line-2
- U11 pad 23: line-10 -> line-7
- U11 pad 24: hv-4 -> hv-2
- U11 pad 4: line-14 -> line-6
- U11 pad 5: line-13 -> line-4
- U11 pad 6: line-17 -> line-8
- U11 pad 7: line-15 -> line-5
- U11 pad 8: line -> line-15
- U11 pad 9: line-7 -> line-10
- U12 pad 1: hv -> hv-3
- U12 pad 3: hv -> hv-3
- U12 pad 5: hv-4 -> hv-2
- U13 pad 1: hv-2 -> hv
- U13 pad 3: hv-2 -> hv
- U13 pad 6: hv-1 -> hv-4
- U2 pad 10: line-7 -> line-10
- U2 pad 4: line-5 -> line-12
- U2 pad 5: line-19 -> line-16
- U2 pad 6: line-3 -> line
- U2 pad 7: line-18 -> line-11
- U2 pad 8: hv -> hv-3
- U2 pad 9: line -> line-15
- U4 pad 4: hv-1 -> hv-4
- U4 pad 5: hv-1 -> hv-4
- U5 pad 2: hv -> hv-3
- U6 pad 1: line-2 -> line-3
- U6 pad 14: line-11 -> line-14
- U6 pad 4: hv -> hv-3
- U6 pad 7: line-4 -> line-13
- U6 pad 8: line-8 -> line-18
- U7 pad 1: hv-4 -> hv-2
- U7 pad 2: line-13 -> line-4
- U7 pad 3: line-14 -> line-6
- U8 pad 1: line-5 -> line-12
- U8 pad 14: line-18 -> line-11
- U8 pad 4: hv -> hv-3
- U8 pad 7: line-19 -> line-16
- U8 pad 8: line-3 -> line
- U9 pad 1: hv-4 -> hv-2
- U9 pad 2: line-15 -> line-5
- U9 pad 3: line-17 -> line-8
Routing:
- net hv-1: track 47.6 -> 0.00 mm, vias 2 -> 0
- net hv-2: track 22.8 -> 67.4 mm, vias 0 -> 9
- net line-1: track 30.5 -> 0.00 mm, vias 2 -> 0
- net line-9: track 0.00 -> 30.1 mm, vias 0 -> 2
- net line-7: track 18.6 -> 47.9 mm
- net line-10: track 47.9 -> 18.6 mm
- net line-2: track 25.2 -> 52.5 mm, vias 0 -> 2
- net line-12: track 0.00 -> 25.3 mm
- net line-17: track 20.9 -> 0.00 mm, vias 2 -> 0
- net hv-4: track 67.4 -> 47.6 mm, vias 9 -> 2
- net line-6: track 52.5 -> 34.2 mm
- net line-4: track 17.0 -> 34.6 mm
- net line-13: track 34.6 -> 17.0 mm
- net hv-3: track 0.00 -> 14.1 mm, vias 0 -> 10
- net line-18: track 37.7 -> 26.6 mm
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- added copper zone on In2.Cu, net hv-2
- added copper zone on F.Cu, net hv-4
- removed copper zone on F.Cu, net hv-1
- removed copper zone on In2.Cu, net hv-4
